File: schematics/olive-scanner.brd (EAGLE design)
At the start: 100 x 80 mm, 14 parts, among them IC1 MCP23008/P

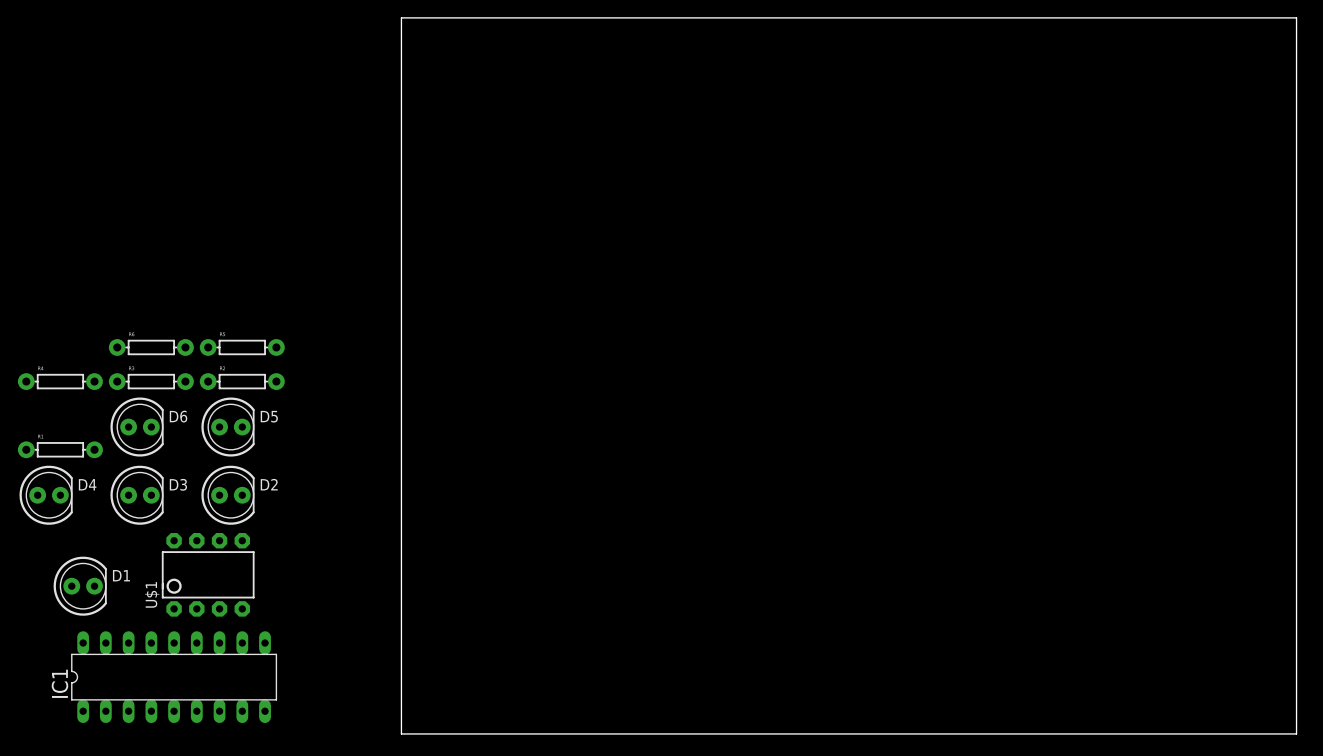
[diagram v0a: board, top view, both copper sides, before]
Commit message: Did the schematics and updated the docs
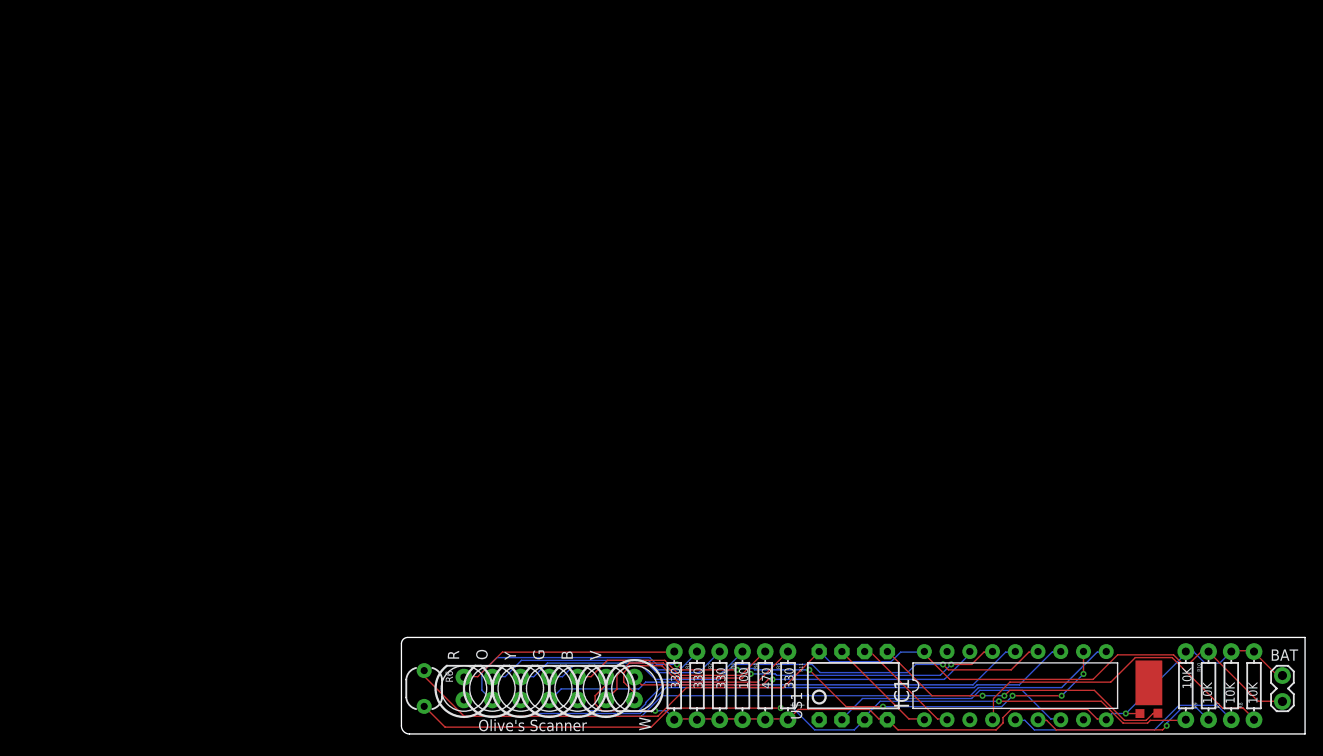
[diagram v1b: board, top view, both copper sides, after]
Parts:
- removed D1, D2, D3, D4, D5, D6: (no value), SparkFun-LED:LED5MM
- added B, G, O, R, V, W, Y: (no value), SparkFun-LED:LED5MM
- added BAT: (no value), SparkFun-Connectors:1X02_LOCK
- added R10, R7, R8, R9: 10K, SparkFun-Resistors:AXIAL-0.3
- added R11: 330, SparkFun-Resistors:AXIAL-0.3
- added U$2: PHONE_VIBRATOR, HokieGeek:PHONE_VIBRATOR
- IC1: value MCP23008/P -> MCP23S08/P; device adafruit:DIL18 -> HokieGeek:DIL18
- R1, R2, R3: value (none) -> 330
- R4: value (none) -> 100
- R5: value (none) -> 470
- R6: value (none) -> PHOTOCELLPTH; device SparkFun-Resistors:AXIAL-0.3 -> SparkFun-Sensors:PHOTOCELL
- moved IC1 94.0 mm to (68.6, 5.40)
- moved R4 83.4 mm to (38.1, 5.40), turned to 270 degrees
- moved R1 73.5 mm to (30.5, 5.40), turned to 270 degrees
- moved U$1 73.1 mm to (50.5, 5.40)
- moved R3 72.0 mm to (35.6, 5.40), turned to 270 degrees
- moved R5 69.6 mm to (40.6, 5.40), turned to 270 degrees
- moved R2 61.1 mm to (33.0, 5.40), turned to 270 degrees
- moved R6 48.8 mm to (2.54, 5.08), turned to 270 degrees
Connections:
- removed net VCC: IC1.18
- new net +3V3: BAT.2, IC1.18, R6.1, R9.P$2, U$1.8
- new net N$1: IC1.4, R8.P$1
- new net N$10: IC1.16, W.A
- new net N$19: IC1.10, R.A
- new net N$2: IC1.6, R9.P$1
- new net N$20: IC1.11, O.A
- new net N$21: IC1.12, Y.A
- new net N$22: G.A, IC1.13
- new net N$23: B.A, IC1.14
- new net N$24: IC1.15, V.A
- new net N$3: IC1.5, R7.P$1
- new net N$4: R.K, R1.P$1
- new net N$5: O.K, R2.P$1
- new net N$6: R3.P$1, Y.K
- new net N$7: G.K, R4.P$1
- new net N$8: B.K, R5.P$1
- new net N$9: R11.P$1, W.K
- new net PB0: U$1.5, U$2.P$2
- new net PB1: IC1.2, U$1.6
- new net PB2: IC1.1, U$1.7
- new net PB3: IC1.7, U$1.2
- new net PB4: R10.P$2, R6.2, U$1.3
- new net PB5: U$1.1
- net GND: now also BAT.1, R1.P$2, R10.P$1, R11.P$2, R2.P$2, R3.P$2, R4.P$2, R5.P$2, R7.P$2, R8.P$2, U$1.4, U$2.P$1, V.K
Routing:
- net +3V3: track 0.00 -> 108.1 mm
- net GND: track 0.00 -> 92.2 mm, vias 0 -> 2
- net PB4: track 0.00 -> 90.6 mm, vias 0 -> 2
- net N$20: track 0.00 -> 77.9 mm, vias 0 -> 7
- net N$19: track 0.00 -> 75.5 mm
- net N$21: track 0.00 -> 63.8 mm
- net N$22: track 0.00 -> 58.1 mm, vias 0 -> 1
- net N$23: track 0.00 -> 52.3 mm
- net N$24: track 0.00 -> 47.8 mm, vias 0 -> 2
- net N$10: track 0.00 -> 39.6 mm, vias 0 -> 1
- net N$1: track 0.00 -> 36.4 mm
- net PB0: track 0.00 -> 34.2 mm, vias 0 -> 2
- net PB3: track 0.00 -> 27.2 mm
- net N$3: track 0.00 -> 26.5 mm
- net N$5: track 0.00 -> 25.0 mm
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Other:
- board size 100 x 80 mm -> 101 x 10.8 mm
- board text added: "20151122"
- board text added: "For Olivia from her Papá"
- board text added: "Olive's Scanner"
